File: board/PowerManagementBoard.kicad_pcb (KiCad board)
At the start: 2 copper layers, 168.7 x 100.6 mm, 148 parts, among them IC1 ACS37010LLZATR-030B3, IC2 ACS37010LLZATR-030B3, IC3 ACS37010LLZATR-030B3, IC4 ACS37010LLZATR-030B3, IC6 ACS37010LLZATR-030B3, J1 RJ45_LED_Shielded, J10 768250002, J11 768250002, J12 768250002, J13 768250002, J14 768250002, J15 768250002, J16 768250002, J17 768250002, J18 768250002, J2 SS-73100-082, J3 SS-73100-082, J5 768250002, J6 768250002, J7 768250002, J8 768250002, J9 768250002, Q1 BSS138, Q2 IPB180N10S4-02, Q3 Si4162DY, Q5 Si4162DY, Q6 Si4162DY, Q7 Si4162DY, Q8 Si4162DY, U1 LT1910, U10 ACS72981LLRATR-100U3, U11 LT1910, U12 LT1910, U13 LT1910, U14 LT1910, U15 Teensy4.1_DEV-16771, U16 OKI-78SR-3.3_1.5-W36H-C, U17 OKI-78SR-5_1.5-W36H-C, U19 LT1910, U4 Opamp_Dual, U5 Opamp_Dual, U6 Opamp_Dual

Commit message: Added Adam
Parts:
- moved G*** 13.6 mm to (161.4, 56.4)
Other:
- board text added: "Honorable mention to our electrical lead: Adam Klassen"

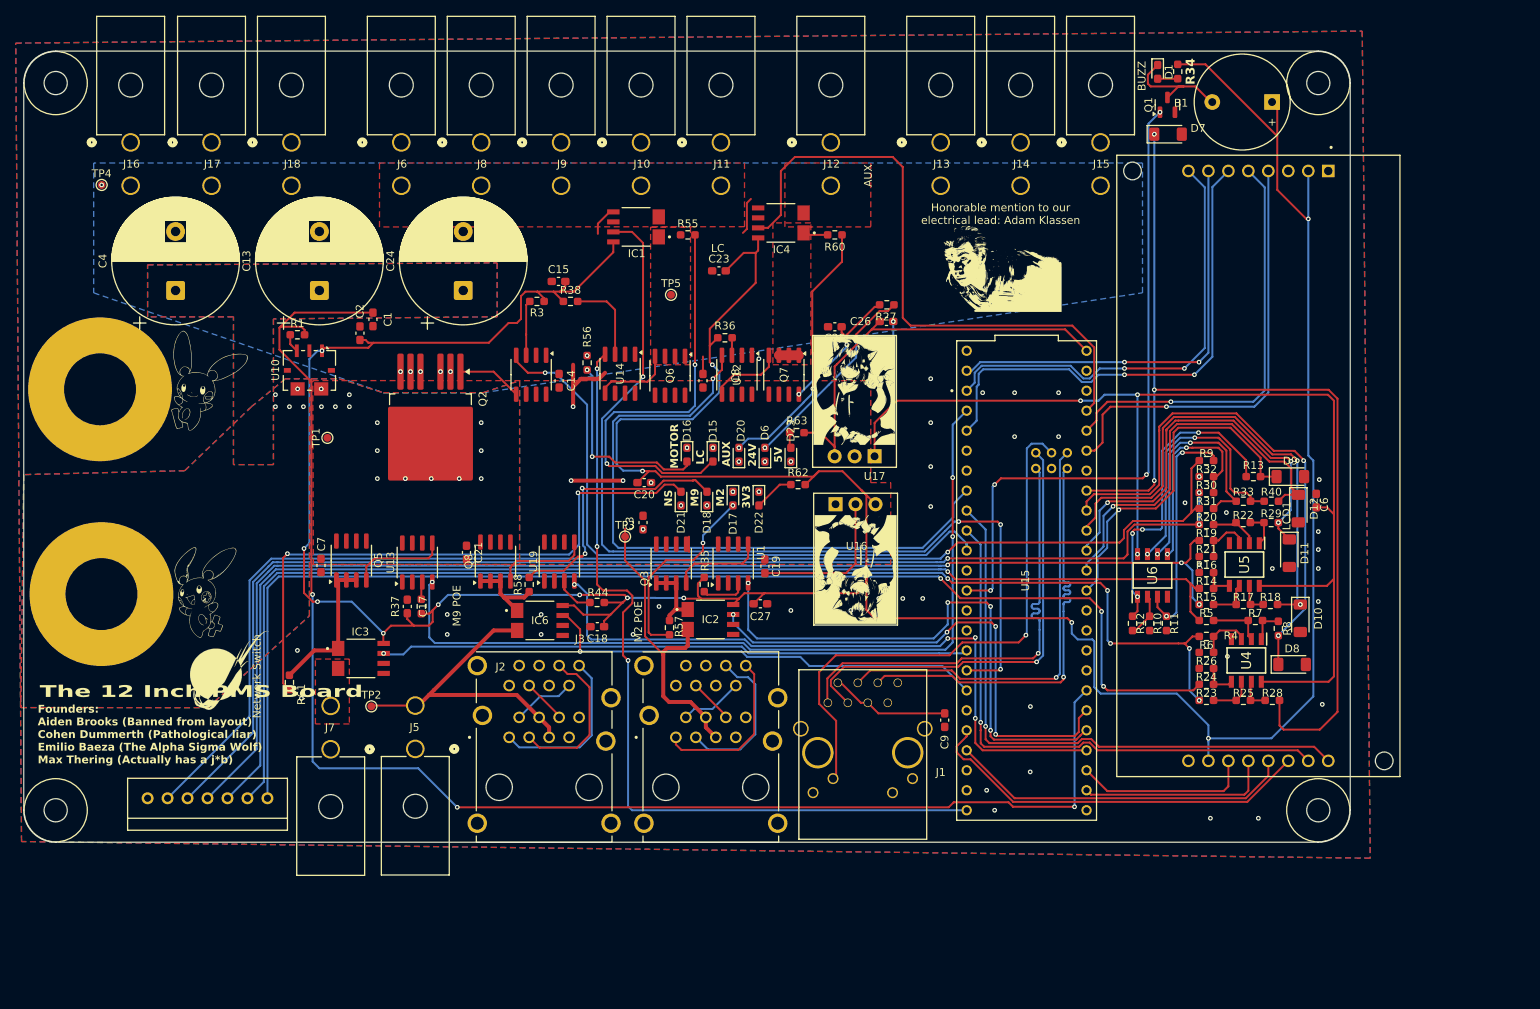
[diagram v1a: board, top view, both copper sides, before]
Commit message: give the board a quick line up
mosfets and drivers in the center are actually aligned well
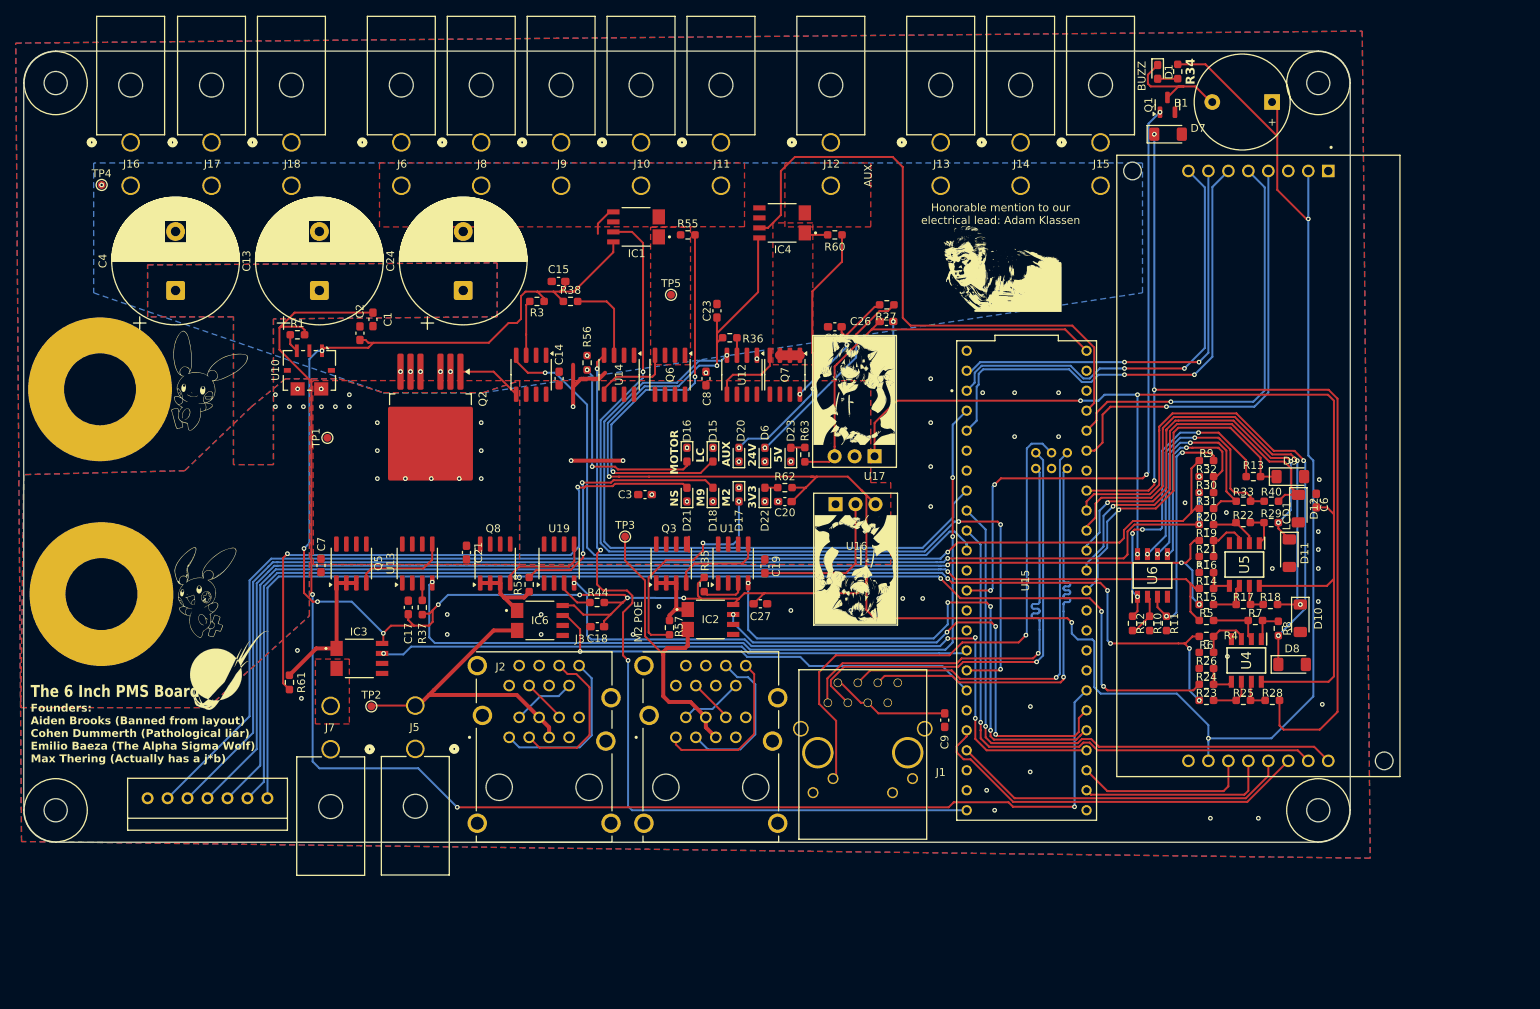
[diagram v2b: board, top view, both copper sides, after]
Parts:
- moved C20 18.0 mm to (136.4, 86.2), turned to 180 degrees
- moved C23 5.09 mm to (127.8, 62.0), turned to 90 degrees
- moved C3 3.57 mm to (118.6, 85.3), turned to 180 degrees
- moved R63 2.97 mm to (138.9, 80.3), turned to 90 degrees
- moved R62 1.72 mm to (136.4, 84.5)
- moved D17 0.92 mm to (130.6, 85.3)
- moved D18 0.92 mm to (127.3, 85.3)
- moved D21 0.92 mm to (124.0, 85.3)
- moved D22 0.92 mm to (133.9, 85.3), turned to 90 degrees
- moved U12 0.64 mm to (130.9, 70.1)
- moved R36 0.61 mm to (129.4, 65.4)
- moved C8 0.47 mm to (126.4, 70.6)
- moved Q5 0.38 mm to (81.3, 94.1)
- moved C14 0.28 mm to (107.7, 70.6)
- moved Q8 0.26 mm to (99.6, 94.1)
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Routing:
- net GND: track 50.4 -> 43.4 mm, vias 58 -> 59
- net Net-(D22-A): track 5.16 -> 1.63 mm
- net Net-(D17-A): track 25.4 -> 28.7 mm
- net Net-(D15-A): track 54.0 -> 51.3 mm
- net +3V3: track 466.3 -> 464.4 mm
- net Net-(D21-A): track 76.1 -> 77.5 mm
- net /Current-Sensinator/m2out: track 38.7 -> 37.7 mm
- net Net-(D18-A): track 33.9 -> 34.8 mm
- net /Current-Sensinator/NSin: track 19.1 -> 18.3 mm
- net Net-(D16-A): track 24.7 -> 25.5 mm
- net /Switching Circuit/AUX_EN: track 84.1 -> 84.8 mm
- net +5V: track 52.6 -> 52.0 mm
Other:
- board text added: "The 6 Inch PMS Board"
- board text removed: "M9 POE"
- board text removed: "Network Switch"
- board text removed: "The 12 Inch PMS Board"

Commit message: Center schematics and layout for prettiness
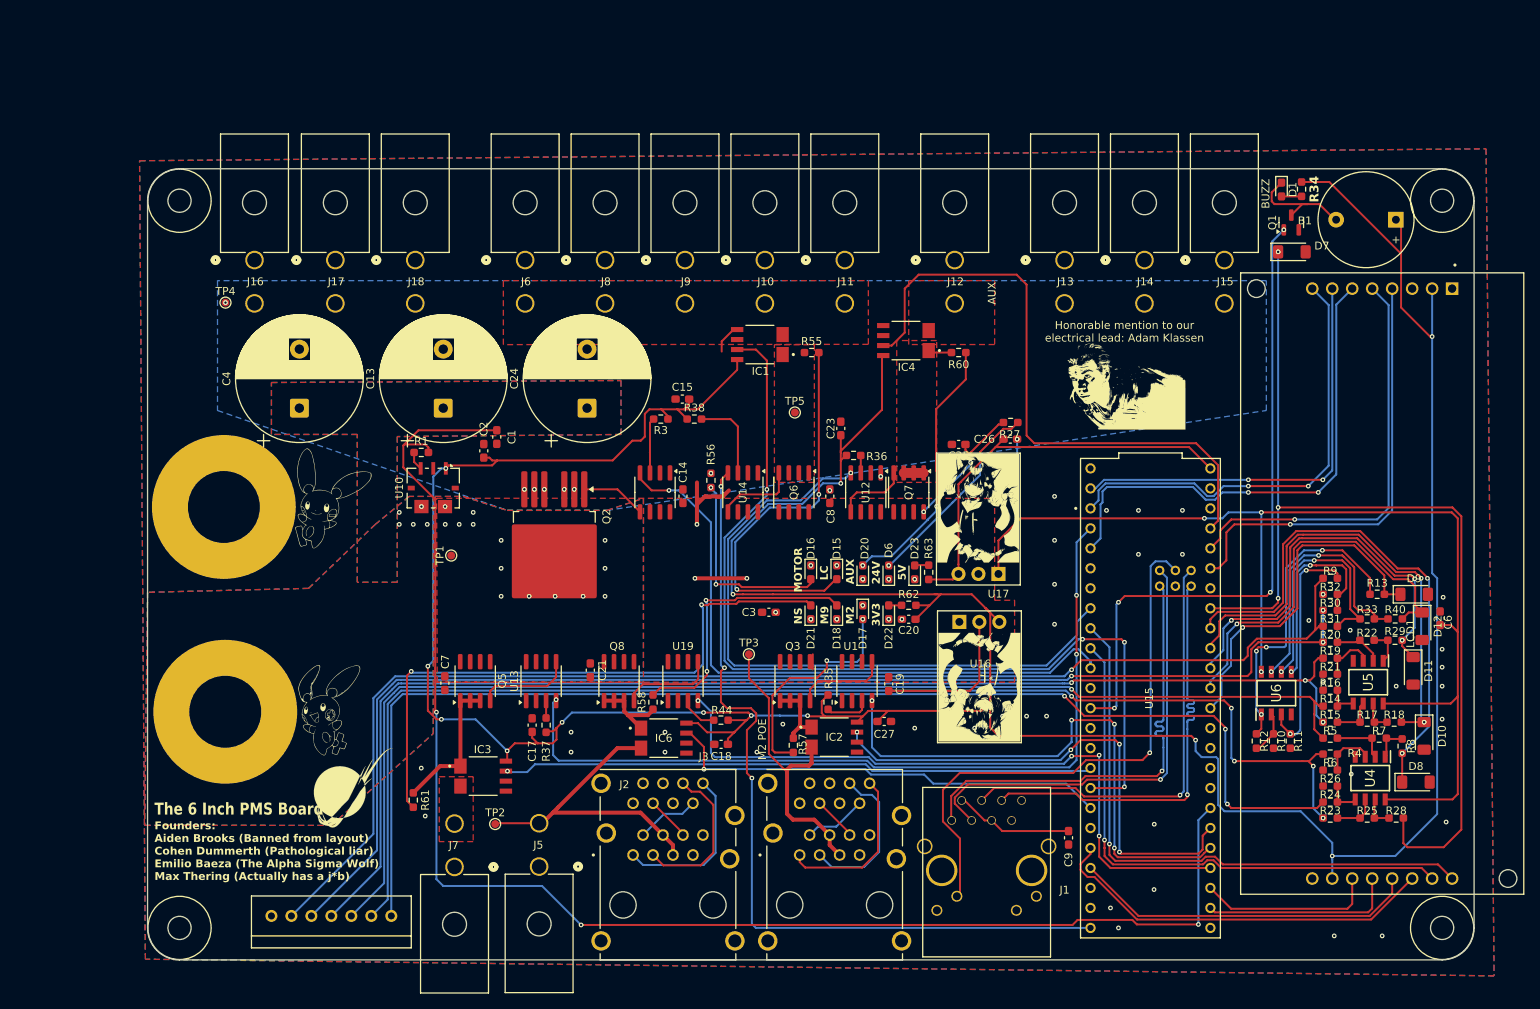
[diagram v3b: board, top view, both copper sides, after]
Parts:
- moved D7 21.7 mm to (200.9, 54.5)
- moved Q1 21.7 mm to (200.8, 50.7)
- moved D11 21.7 mm to (216.3, 107.8)
- moved D12 21.7 mm to (217.4, 102.1)
- moved U6 21.7 mm to (198.9, 110.6)
- moved C18 21.7 mm to (128.3, 117.1)
- moved C8 21.7 mm to (142.1, 85.5)
- moved Conn1 21.7 mm to (86.4, 138.9)
- moved Q2 21.7 mm to (107.1, 92.3)
- moved R57 21.7 mm to (137.5, 117.2)
- moved C13 21.7 mm to (93.0, 74.4)
- moved J10 21.7 mm to (133.9, 55.5)
- moved C14 21.7 mm to (123.4, 85.5)
- moved C15 21.7 mm to (123.4, 73.2)
- moved C17 21.7 mm to (104.3, 114.7)
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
